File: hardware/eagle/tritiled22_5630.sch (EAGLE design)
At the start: 15 parts, among them Q1 ZXMN3B01FTA, Q2 DMG2305UX, SW1 SMD_SWITCH, U1 PIC12LF1571

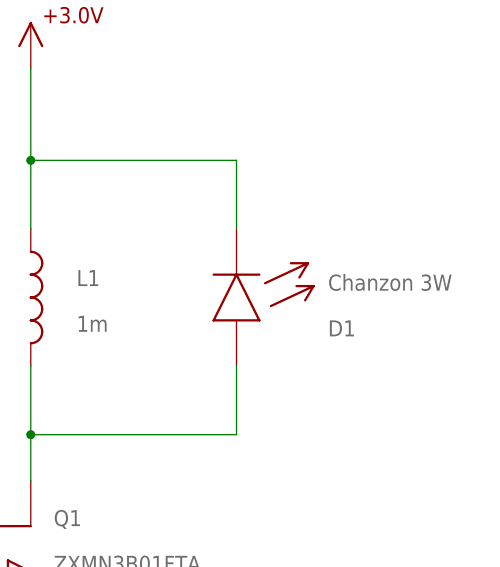
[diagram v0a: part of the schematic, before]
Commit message: Added new LED eiditons: 5630, Luxeon C, Luxeon Z fixed inconsistent C2 value: now should be 100n everywhere
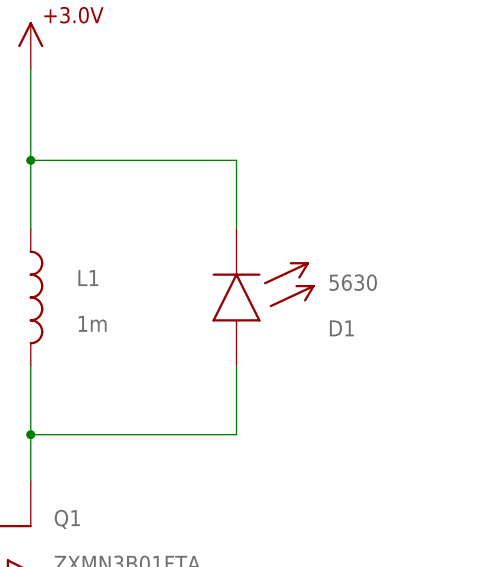
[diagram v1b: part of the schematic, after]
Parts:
- D1: value Chanzon 3W -> 5630; device tritiled:LED_3W -> tritiled:LED5630
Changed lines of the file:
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@@
 <part name="U$8" library="z0" deviceset="GND" device=""/>
 <part name="U$11" library="z0" deviceset="GND" device=""/>
-<part name="D1" library="tritiled" deviceset="LED_3W" device="" value="Chanzon 3W"/>
+<part name="D1" library="tritiled" deviceset="LED" device="5630" value="5630"/>
 <part name="L1" library="tritiled" deviceset="SRR6028_INDUCTOR" device="" value="1m"/>
 <part name="U$13" library="tritiled" deviceset="+3.0V" device=""/>
